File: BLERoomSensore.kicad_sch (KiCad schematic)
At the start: 7 parts, among them J1 FTSH-105-01-F-DV-P-TR, U2 BME280, U3 BMD-360-A-R

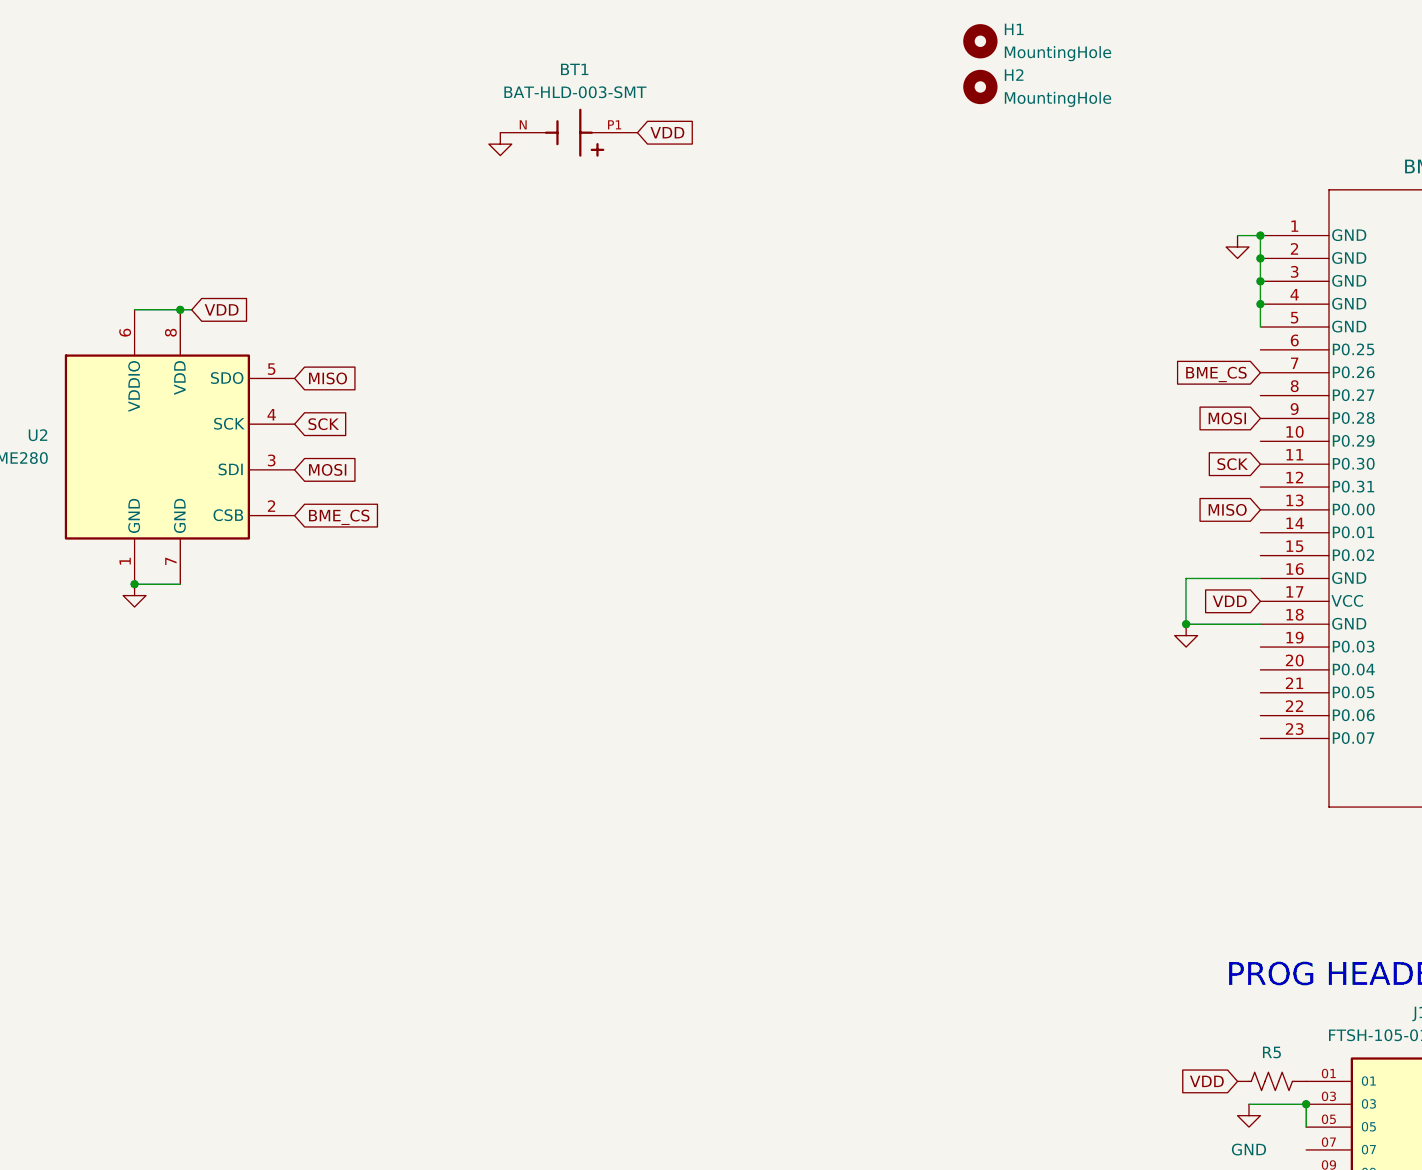
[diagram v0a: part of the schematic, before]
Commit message: Updated sch with ACC and RTK
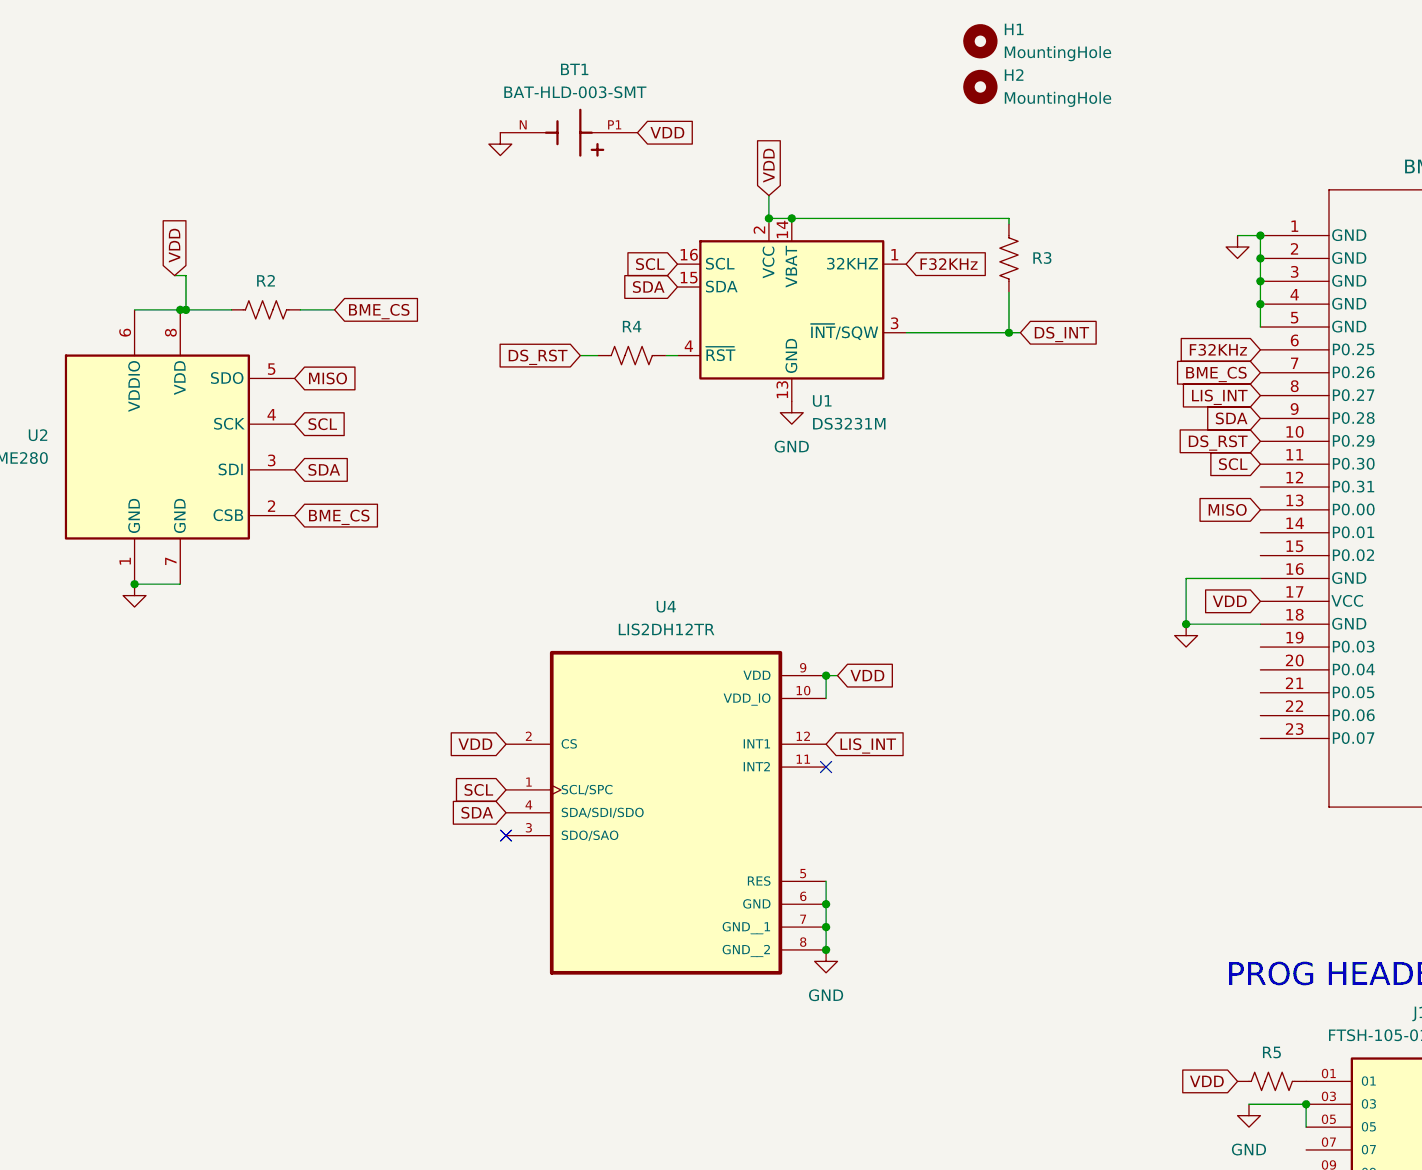
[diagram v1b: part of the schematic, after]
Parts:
- added R2, R3, R4: 10k, Resistor_SMD:R_0603_1608Metric_Pad0.98x0.95mm_HandSolder, symbol Device:R_US
- added U1: DS3231M, Package_SO:SOIC-16W_7.5x10.3mm_P1.27mm, symbol Timer_RTC:DS3231M
- added U4: LIS2DH12TR, LIS2DH12TR:PQFN50P200X200100-12N, symbol LIS2DH12TR:LIS2DH12TR
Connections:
- net BME_CS: now also R2.2
- net GND: now also U1.10 (GND), U1.11 (GND), U1.12 (GND), U1.13 (GND), U1.5 (GND), U1.6 (GND), U1.7 (GND), U1.8 (GND), U1.9 (GND), U4.5 (RES), U4.6 (GND), U4.7 (GND__1), U4.8 (GND__2)
- net VDD: now also R2.1, R3.2, U1.14 (VBAT), U1.2 (VCC), U4.10 (VDD_IO), U4.2 (CS), U4.9 (VDD)
- net DS_RST: now reaches U3.10 (P0.29)
- net DS_RST: now also R4.2
- net F32KHz: now reaches U3.6 (P0.25)
- net F32KHz: now also U1.1 (32KHZ)
- net LIS_INT: now reaches U3.8 (P0.27)
- net LIS_INT: now also U4.12 (INT1)
- net MOSI renamed SDA
- net SDA: now also U1.15 (SDA), U4.4 (SDA/SDI/SDO)
- net SCK renamed SCL
- net SCL: now also U1.16 (SCL), U4.1 (SCL/SPC)
- new net: R4.1, U1.4 (~{RST})
- new net DS_INT: R3.1, U1.3 (~{INT}/SQW)
- no-connect marks 0 -> 2

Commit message: Routing Done, no DRC errors
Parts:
- removed BT1: BAT-HLD-003-SMT, BAT_HLD_003_SMT:BAT_BAT-HLD-003-SMT, symbol BAT-HLD-003-SMT:BAT-HLD-003-SMT
- removed R4: 10k, Resistor_SMD:R_0603_1608Metric_Pad0.98x0.95mm_HandSolder, symbol Device:R_US
- removed U1: DS3231M, Package_SO:SOIC-16W_7.5x10.3mm_P1.27mm, symbol Timer_RTC:DS3231M
- added BT1: Battery_Cell, BAT_HLD_003_SMT:BAT_BAT-HLD-003-SMT_MOD, symbol Device:Battery_Cell
- added U5: PCF8523TK, Package_SON:HVSON-8-1EP_4x4mm_P0.8mm_EP2.2x3.1mm, symbol Timer_RTC:PCF8523TK
- added XTAL1: FC-135 32.7680KA-A3, XTAL_FC-135R_EPS, symbol 2025-02-09_19-16-04:FC-135_32.7680KA-A3
- R2, R3, R5: footprint Resistor_SMD:R_0603_1608Metric_Pad0.98x0.95mm_HandSolder -> Resistor_SMD:R_0402_1005Metric_Pad0.72x0.64mm_HandSolder
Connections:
- net DS_INT is gone; now on net PCF_INT: R3.1
- net GND: now also U2.5 (SDO), BT1.2 (-), U5.4 (VSS), U5.9 (VSS)
- net LIS_INT: now also U3.13 (P0.00); no longer U3.8 (P0.27)
- net SCL: now also U5.6 (SCL)
- net SDA: now also U5.5 (SDA)
- net VDD: now also BT1.1 (+), U5.3 (VBAT), U5.8 (VDD)
- net PCF_INT: now reaches U3.15 (P0.02)
- net PCF_INT: now also U5.7 (~{INT1}/CLKOUT)
- net DS_RST: no longer names the net of U3.10 (P0.29)
- net F32KHz: no longer names the net of U3.6 (P0.25)
- removed net MISO: U2.5 (SDO), U3.13 (P0.00)
- new net: U5.1 (OSCI), XTAL1.1
- new net: U5.2 (OSCO), XTAL1.2

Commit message: Add expansion header
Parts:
- added EXP1: Conn_01x04_Pin, Connector_PinHeader_1.00mm:PinHeader_1x04_P1.00mm_Vertical, symbol Connector:Conn_01x04_Pin
- added R4, R5: 10k, Resistor_SMD:R_0402_1005Metric_Pad0.72x0.64mm_HandSolder, symbol Device:R_US
- added TP_LIS1: TestPoint, TestPoint:TestPoint_Pad_D1.0mm, symbol Connector:TestPoint
- R2, R3: value 10k -> 100k; Digikey P/N YAG1290CT-ND -> (none); Manufacturer P/N RC0603FR-0710KP -> (none); Price 0.10 -> (none); Seeed Alt. 301010299 -> (none)
- R5: value 10k -> 0; Digikey P/N YAG1290CT-ND -> (none); Manufacturer P/N RC0603FR-0710KP -> (none); Price 0.10 -> (none); Seeed Alt. 301010299 -> (none)
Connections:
- net GND: now also EXP1.1 (Pin_1), R4.1, R5.1
- net LIS_INT: now also TP_LIS1.1
- net SCL: now also R5.2
- net SDA: now also R4.2
- net at U3.31 (P0.13): now also EXP1.2 (Pin_2)
- net at U3.33 (P0.15): now also EXP1.3 (Pin_3)
- net at U3.35 (P0.17): now also EXP1.4 (Pin_4)

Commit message: BOM
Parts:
- BT1: JPN (none) -> C964829; MFR (none) -> MYOUNG; MPN (none) -> MY-2032-05
- EXP1, H1, H2, TP_LIS1: now left out of the parts list
- J1: JPN (none) -> C5886427; MFR (none) -> GCT; MPN (none) -> BD125-10-A-0305-0580-L-B; Manufacturer P/N BD125-10-A-0305-0580-L-B -> (none)
- R2, R3: JPN (none) -> C60491; MFR (none) -> YAGEO; MPN (none) -> RC0402FR-07100KL
- R4, R5: JPN (none) -> C60489; MFR (none) -> YAGEO; MPN (none) -> RC0402JR-0710KL
- R5: JPN (none) -> C60485; MFR (none) -> YAGEO; MPN (none) -> RC0402JR-070RL
- U2: JPN (none) -> C92489; MFR (none) -> Bosch Sensortec; MPN (none) -> BME280
- U3: JPN (none) -> C9900022355; MPN (none) -> BMD-360-A-R; MRF (none) -> U-BLOX
- U4: JPN (none) -> C110926; MF STMicroelectronics -> (none); MFR (none) -> STMicroelectronics; MP LIS2DH12TR -> (none); MPN (none) -> LIS2DH12TR
- U5: JPN (none) -> C2651518; MFR (none) -> NXP Semicon; MPN (none) -> PCF8523TK
- XTAL1: JPN (none) -> C2236; MFR (none) -> YXC Crystal Oscillators

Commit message: Bunch o production files
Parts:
- removed J1: FTSH-105-01-F-DV-P-TR, FTSH-105-01-F-DV-P-TR:SAMTEC_FTSH-105-01-F-DV-P-TR, symbol FTSH-105-01-F-DV-P-TR:FTSH-105-01-F-DV-P-TR
- removed R5: 0, Resistor_SMD:R_0402_1005Metric_Pad0.72x0.64mm_HandSolder, symbol Device:R_US
- removed U5: PCF8523TK, Package_SON:HVSON-8-1EP_4x4mm_P0.8mm_EP2.2x3.1mm, symbol Timer_RTC:PCF8523TK
- added J2: Conn_ARM_SWD_TagConnect_TC2030-NL, Connector:Tag-Connect_TC2030-IDC-NL_2x03_P1.27mm_Vertical, symbol Connector:Conn_ARM_SWD_TagConnect_TC2030-NL
- added R1: 0, Resistor_SMD:R_0402_1005Metric_Pad0.72x0.64mm_HandSolder, symbol Device:R_US
- added U5: PCF8523T, Package_SO:SOIC-8_3.9x4.9mm_P1.27mm, symbol Timer_RTC:PCF8523T
- XTAL1: JPN C2236 -> C1985290; MFR YXC Crystal Oscillators -> Seiko Epson; MPN X206032768KGB2SC -> FC-12M 32.7680KA-A3
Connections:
- net CLK: now also J2.4 (SWCLK)
- net DIO: now also J2.2 (SWDIO)
- net GND: now also J2.5 (GND), U5.4 (VSS)
- net PCF_INT: now also U5.7 (~{INT1}/CLKOUT)
- net RESET: now also J2.3 (~{RESET})
- net SCL: now also U5.6 (SCL)
- net SDA: now also U5.5 (SDA)
- net VDD: now also R1.2, U5.3 (VBAT), U5.8 (VDD)
- net at XTAL1.1: now also U5.1 (OSCI)
- net at XTAL1.2: now also U5.2 (OSCO)
- new net: J2.1 (VCC), R1.1

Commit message: Working on comp changes
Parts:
- removed U3: BMD-360-A-R, BMD-360_UBL, symbol BMD-360-A-R:BMD-360-A-R
- added AE1: 2450AT18A100E, Capacitor_SMD:C_0603_1608Metric, symbol Device:Antenna_Chip
- added C1, C2, C3, C4: 100nF X7S, Capacitor_SMD:C_0402_1005Metric_Pad0.74x0.62mm_HandSolder, symbol Device:C
- added C10: 4.7uF X7R, Capacitor_SMD:C_0603_1608Metric_Pad1.08x0.95mm_HandSolder, symbol Device:C
- added C11: 1pF NP0, Capacitor_SMD:C_0402_1005Metric_Pad0.74x0.62mm_HandSolder, symbol Device:C
- added C12: 1.2pF NP0, Capacitor_SMD:C_0402_1005Metric_Pad0.74x0.62mm_HandSolder, symbol Device:C
- added C5, C6: 0.1uF X7S, Capacitor_SMD:C_0402_1005Metric_Pad0.74x0.62mm_HandSolder, symbol Device:C
- added C7: 100pF NP0, Capacitor_SMD:C_0402_1005Metric_Pad0.74x0.62mm_HandSolder, symbol Device:C
- added C8, C9: 12pF NP0, Capacitor_SMD:C_0402_1005Metric_Pad0.74x0.62mm_HandSolder, symbol Device:C
- added L1: 4.7nH, Inductor_SMD:L_0402_1005Metric, symbol Device:L
- added L2: 2.2nH, Inductor_SMD:L_0402_1005Metric, symbol Device:L
- added U1: nRF52833_QDxx, Package_DFN_QFN:QFN-40-1EP_5x5mm_P0.4mm_EP3.6x3.6mm, symbol MCU_Nordic:nRF52833_QDxx
- added Y1: X201632MOB4SI, Crystal:Crystal_SMD_2016-4Pin_2.0x1.6mm, symbol Device:Crystal_GND24
- EXP1: footprint Connector_PinHeader_1.00mm:PinHeader_1x04_P1.00mm_Vertical -> Connector_PinHeader_1.27mm:PinHeader_1x04_P1.27mm_Vertical
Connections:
- net BME_CS: now also U1.31 (AIN1/P0.03)
- net CLK: now also U1.20 (SWDCLK)
- net DIO: now also U1.19 (SWDIO)
- net GND: now also C1.2, C10.1, C11.1, C12.1, C2.1, C3.1, C4.1, C5.1, C6.1, C7.1, C8.1, C9.2, U1.10 (VBUS), U1.25 (VSS_PA), U1.37 (VSS), U1.41 (VSS), Y1.2, Y1.4
- net LIS_INT: now also U1.35 (AIN6/P0.30)
- net PCF_INT: now also U1.36 (AIN7/P0.31)
- net RESET: now also U1.16 (P0.18/~{RESET})
- net SCL: now also U1.34 (AIN5/P0.29)
- net SDA: now also U1.33 (AIN4/P0.28)
- net VDD: now also C10.2, C2.2, C3.2, C6.2, U1.18 (VDD), U1.30 (VDD), U1.40 (VDD), U1.8 (VDD), U1.9 (VDDH)
- net at EXP1.2 (Pin_2): now also U1.14 (P0.15)
- net at EXP1.3 (Pin_3): now also U1.15 (P0.17)
- net at EXP1.4 (Pin_4): now also U1.17 (P0.20)
- new net: C1.1, U1.1 (DEC1)
- new net: C11.2, L1.2, U1.24 (ANT)
- new net: C8.2, U1.28 (XC1), Y1.1
- new net: C9.1, U1.29 (XC2), Y1.3
- new net: AE1.2 (PCB_Trace), L2.1
- new net: C12.2, L1.1, L2.2
- new net DEC3: C7.2, U1.27 (DEC3)
- new net DEC4_6: C5.2, U1.26 (DEC6), U1.38 (DEC4)
- new net DEC5: C4.2, U1.21 (DEC5)
- no-connect marks 2 -> 16
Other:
- moved on the sheet: J2, R1, R4, R5
